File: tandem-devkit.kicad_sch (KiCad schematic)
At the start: 18 parts, among them J101 Conn_01x02

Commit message: Pre routing: footprints&parts
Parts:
- removed R104, R108, R109: 22, Resistor_SMD:R_0603_1608Metric, symbol Device:R
- added R114, R115: 15k, Resistor_SMD:R_0603_1608Metric, symbol Device:R
- added R? (x3): 22, Resistor_SMD:R_0603_1608Metric, symbol Device:R
- J102: renamed from J?; value QWIC I2C Connector -> QWIIC I2C Connector; footprint (none) -> project-lib:JST_SHL_SM04B-SHLS-TF_1x04-1MP_P1.00mm_Horizontal; symbol Connector_Generic:Conn_01x02 -> Connector_Generic:Conn_01x04; JLCPCB (none) -> C145956
- gave numbers to parts that had none: 2
- renumbered R110 to R112, R111 to R113
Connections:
- net CAP_TOUCH_1: now also A101.5 (A0), A102.5 (A0); no longer A101.6 (A1), A102.6 (A1)
- net EPD_BL: now also R?.1
- net EPD_CURRENT_SENSE: now also A101.6 (A1), A102.6 (A1); no longer A101.7 (A2), A102.7 (A2)
- net GND: now also J102.4 (Pin_4)
- net I2C_SCL: now also J102.1 (Pin_1), R115.2
- net I2C_SDA: now also J102.2 (Pin_2), R114.2
- net LCD_BL: now also R?.1
- net LCD_CURRENT_SENSE: now also A101.7 (A2), A102.7 (A2); no longer A101.8 (A3), A102.8 (A3)
- net LCD_DISP: now also R?.1
- net VCC: now also J102.3 (Pin_3), R114.1, R115.1
- net at A101.10 (A5), A102.10 (A5): now also R?.2; no longer R113.2
- net at A101.20 (D7), A102.20 (D6): now also R?.2
- net at A101.23 (D11), A102.23 (D11): now also R?.2
- net at A101.9 (A4), A102.9 (A4): now also R113.2; no longer R112.2
- new net: A101.8 (A3), A102.8 (A3), R112.2
- no-connect marks 5 -> 3
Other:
- moved on the sheet: R112, R113, TP101

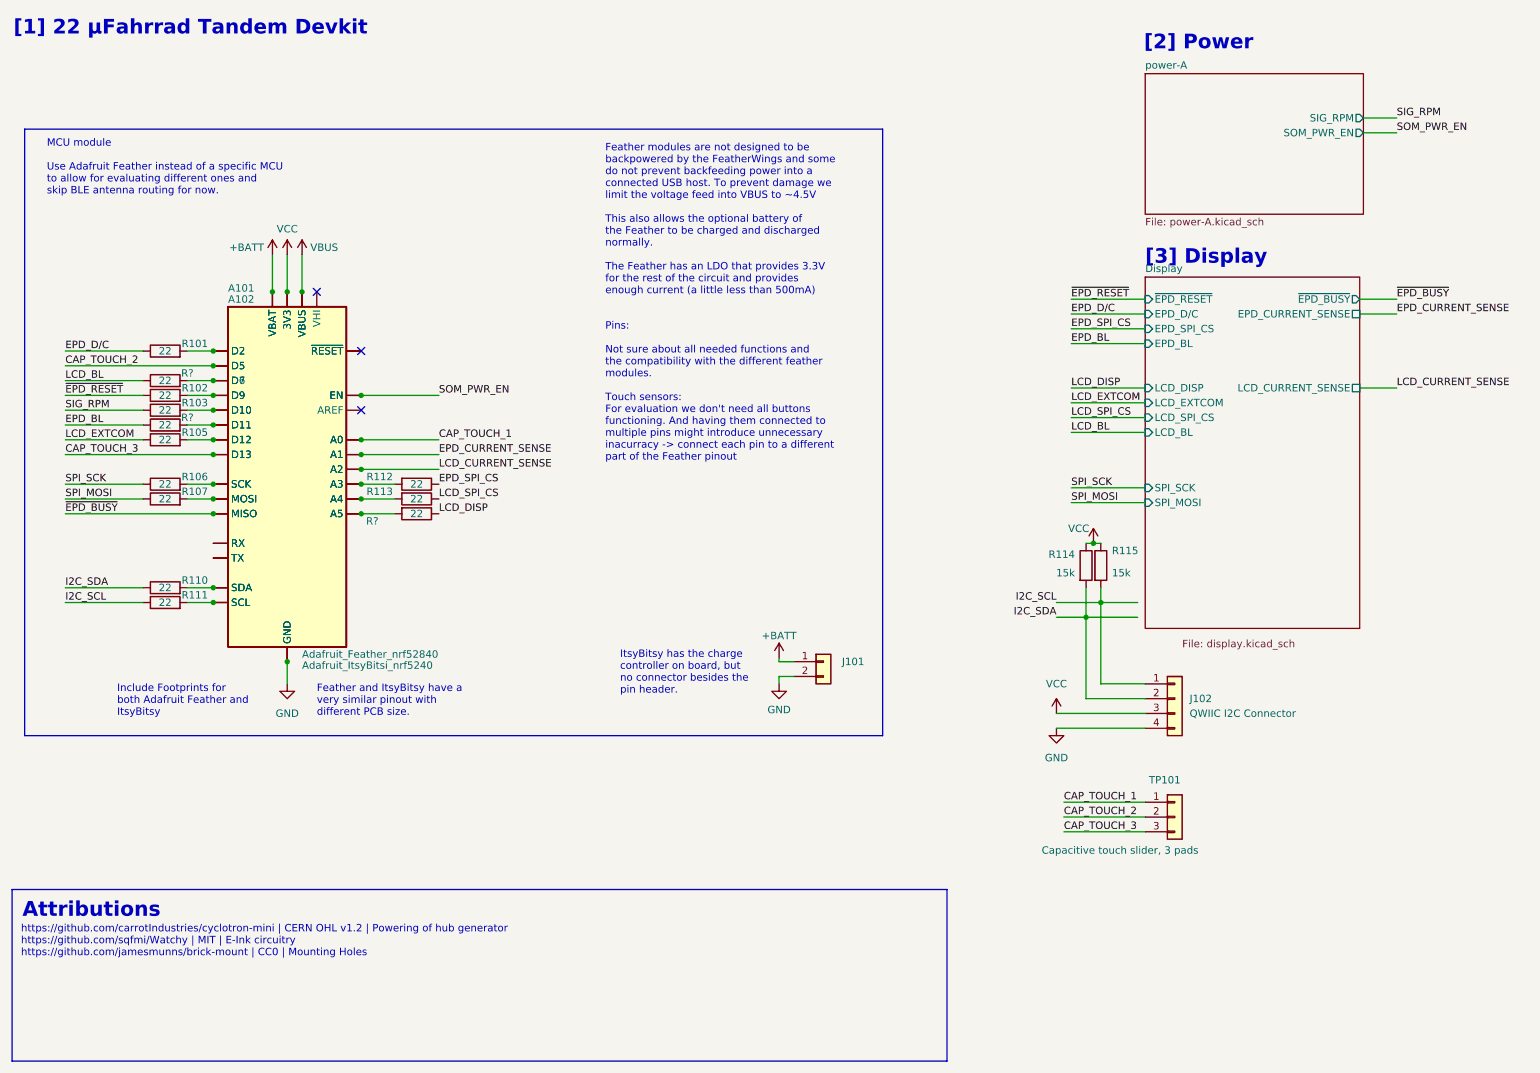
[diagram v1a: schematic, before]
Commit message: Schematics: Add mountingpins to connectors, remove ERC warnings for alternate parts
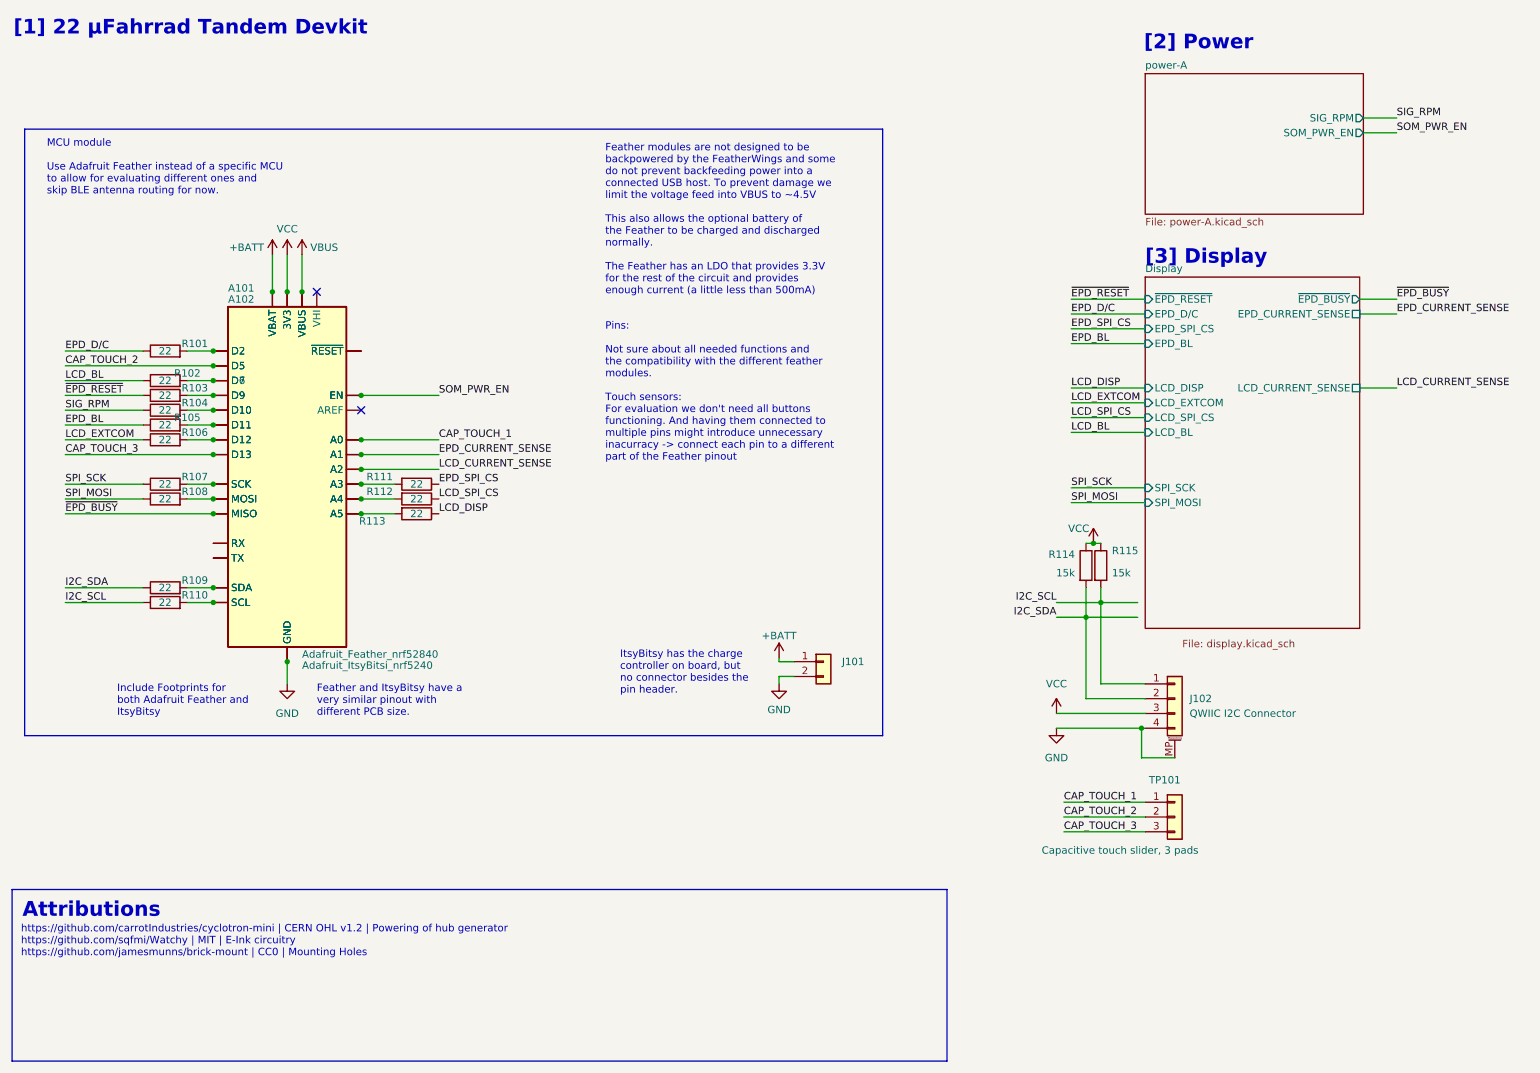
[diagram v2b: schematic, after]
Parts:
- A101: symbol project-lib:Adafruit_ItsyBitsi_nrf5240 -> project-lib:Adafruit_ItsyBitsi_nrf5240-pins-passive
- J102: symbol Connector_Generic:Conn_01x04 -> Connector_Generic_MountingPin:Conn_01x04_MountingPin
- gave numbers to parts that had none: 3
- renumbered R102 to R103, R103 to R104, R105 to R106, R106 to R107, R107 to R108, R110 to R109, R111 to R110, R112 to R111, R113 to R112
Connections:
- net GND: now also J102.MP (MountPin)
- no-connect marks 3 -> 2
